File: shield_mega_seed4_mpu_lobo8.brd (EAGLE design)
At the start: 99.4 x 72.4 mm, 32 parts, among them U1 GY-521MPU6050

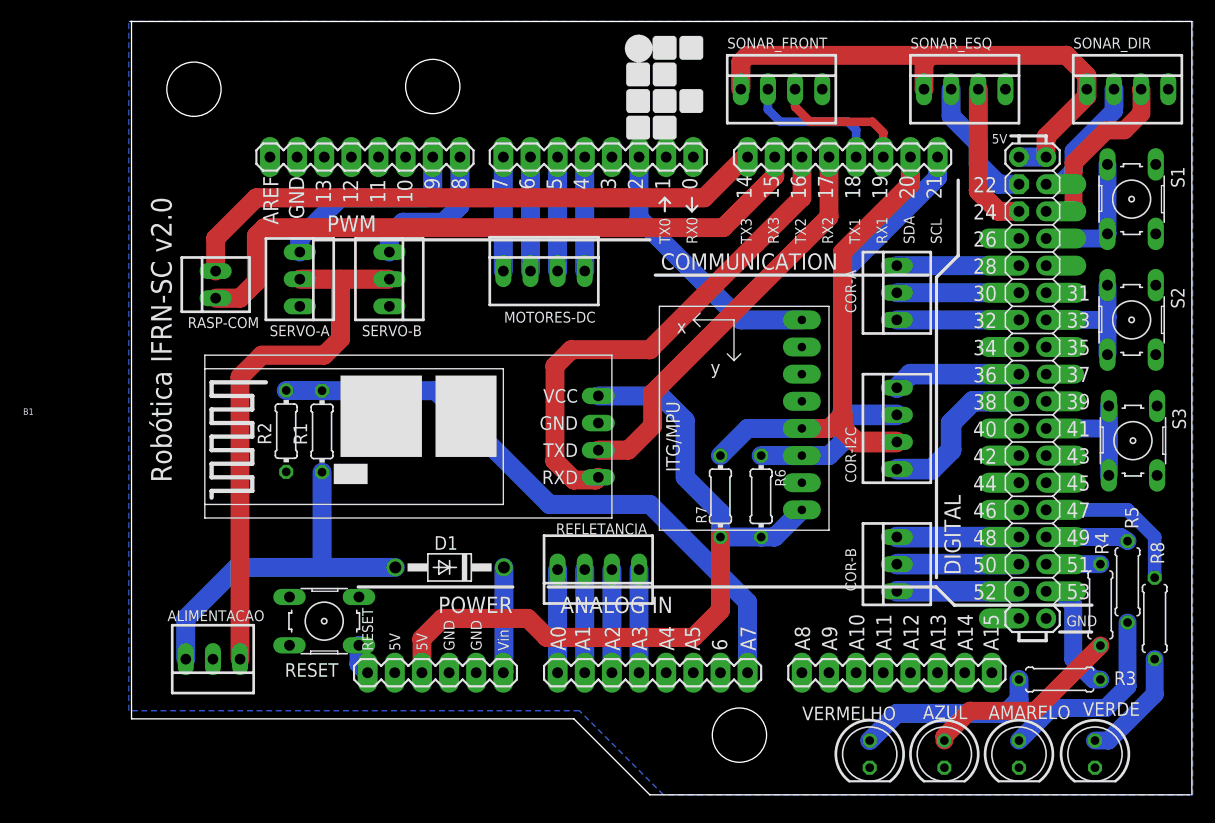
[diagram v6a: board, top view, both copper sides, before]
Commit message: Mudança no tamanho da placa.
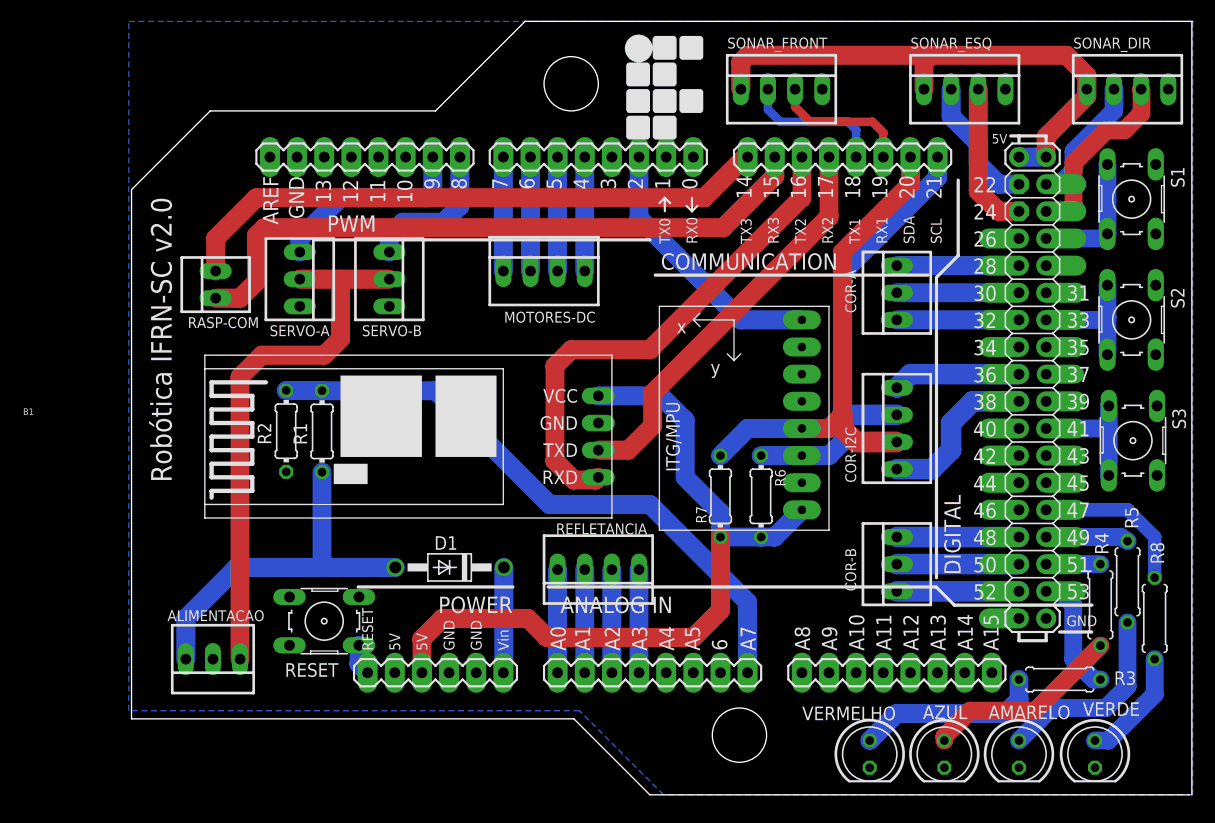
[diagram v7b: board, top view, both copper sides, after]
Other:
- board size 99.4 x 72.4 mm -> 99.3 x 72.4 mm
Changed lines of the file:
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@@
 <layer number="20" name="Dimension" color="15" fill="1" visible="yes" active="yes"/>
 <layer number="21" name="tPlace" color="7" fill="1" visible="yes" active="yes"/>
-<layer number="22" name="bPlace" color="7" fill="1" visible="no" active="yes"/>
+<layer number="22" name="bPlace" color="7" fill="1" visible="yes" active="yes"/>
 <layer number="23" name="tOrigins" color="15" fill="1" visible="yes" active="yes"/>
 <layer number="24" name="bOrigins" color="15" fill="1" visible="yes" active="yes"/>
@@
 <plain>
 <wire x1="98.73" y1="8.89" x2="98.73" y2="81.27" width="0" layer="20"/>
-<wire x1="98.73" y1="81.27" x2="-0.635" y2="81.27" width="0" layer="20"/>
 <rectangle x1="45.9867" y1="70.2183" x2="47.8155" y2="70.2437" layer="21"/>
 <rectangle x1="48.4759" y1="70.2183" x2="50.3047" y2="70.2437" layer="21"/>
@@
 <text x="1.3208" y="64.84111875" size="1.9304" layer="21" font="vector" rot="R270">   Robótica IFRN-SC v2.0</text>
 <hole x="56.388" y="14.478" drill="5.08"/>
-<hole x="27.686" y="75.184" drill="5.08"/>
-<hole x="5.334" y="74.93" drill="5.08"/>
+<hole x="40.64" y="75.438" drill="5.08"/>
 <wire x1="98.552" y1="8.89" x2="48.006" y2="8.89" width="0" layer="20"/>
 <wire x1="48.006" y1="8.89" x2="40.894" y2="16.002" width="0" layer="20"/>
 <wire x1="40.894" y1="16.002" x2="-0.508" y2="16.002" width="0" layer="20"/>
-<wire x1="-0.508" y1="16.002" x2="-0.508" y2="81.28" width="0" layer="20"/>
+<wire x1="-0.508" y1="16.002" x2="-0.508" y2="65.532" width="0" layer="20"/>
+<wire x1="98.806" y1="81.28" x2="36.322" y2="81.28" width="0" layer="20"/>
+<wire x1="6.858" y1="72.898" x2="-0.508" y2="65.532" width="0" layer="20"/>
+<wire x1="27.94" y1="72.898" x2="36.322" y2="81.28" width="0" layer="20"/>
+<wire x1="6.858" y1="72.898" x2="27.94" y2="72.898" width="0" layer="20"/>
 </plain>
 <attributes>

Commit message: Modificação do tamanho mínimo da trilha de terra; Modificação de trilha que estava torta para ficar reta
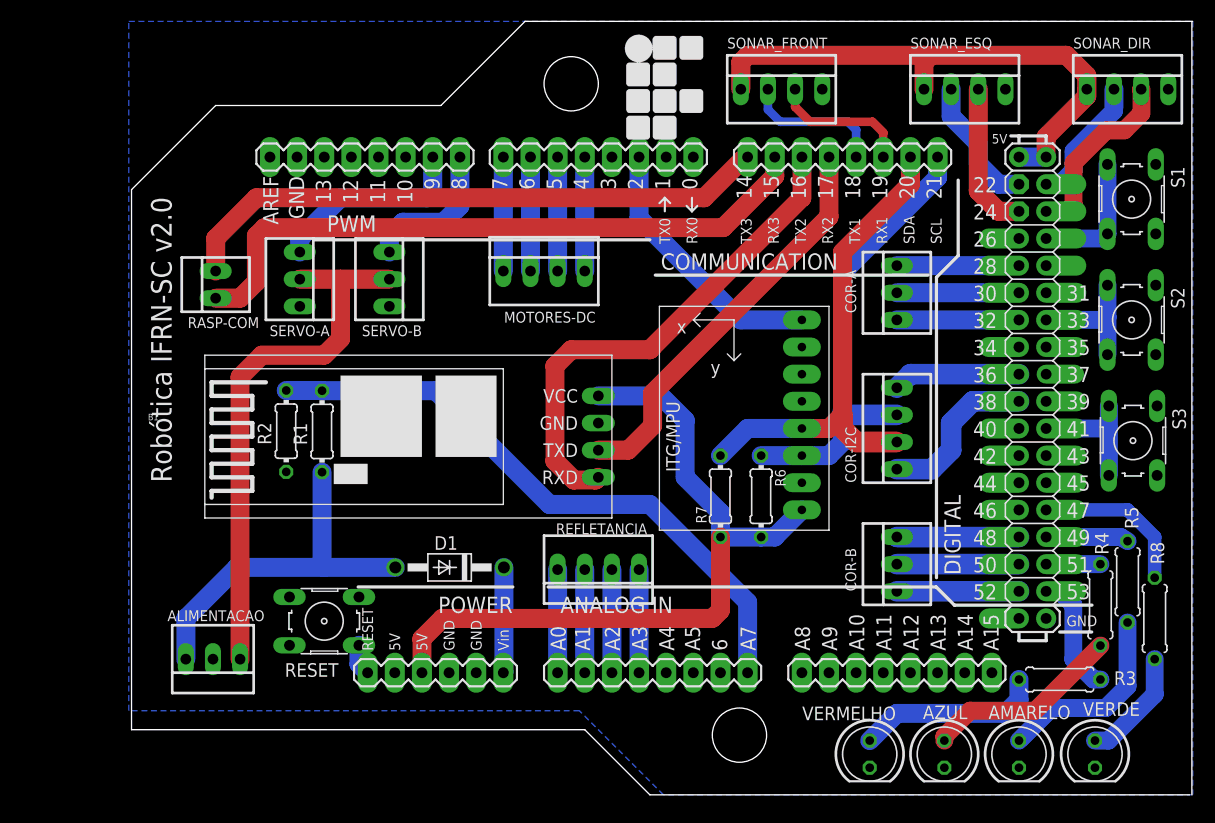
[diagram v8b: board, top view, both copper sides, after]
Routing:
- net +5V/1: track 70.6 -> 69.1 mm
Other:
- outline, holes or cut-outs redrawn
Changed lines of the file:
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@@
 <layer number="20" name="Dimension" color="15" fill="1" visible="yes" active="yes"/>
 <layer number="21" name="tPlace" color="7" fill="1" visible="yes" active="yes"/>
-<layer number="22" name="bPlace" color="7" fill="1" visible="yes" active="yes"/>
+<layer number="22" name="bPlace" color="7" fill="1" visible="no" active="yes"/>
 <layer number="23" name="tOrigins" color="15" fill="1" visible="yes" active="yes"/>
 <layer number="24" name="bOrigins" color="15" fill="1" visible="yes" active="yes"/>
@@
 <hole x="40.64" y="75.438" drill="5.08"/>
 <wire x1="98.552" y1="8.89" x2="48.006" y2="8.89" width="0" layer="20"/>
-<wire x1="48.006" y1="8.89" x2="40.894" y2="16.002" width="0" layer="20"/>
-<wire x1="40.894" y1="16.002" x2="-0.508" y2="16.002" width="0" layer="20"/>
-<wire x1="-0.508" y1="16.002" x2="-0.508" y2="65.532" width="0" layer="20"/>
+<wire x1="48.006" y1="8.89" x2="41.91" y2="14.986" width="0" layer="20"/>
+<wire x1="-0.508" y1="14.986" x2="-0.508" y2="65.532" width="0" layer="20"/>
 <wire x1="98.806" y1="81.28" x2="36.322" y2="81.28" width="0" layer="20"/>
-<wire x1="6.858" y1="72.898" x2="-0.508" y2="65.532" width="0" layer="20"/>
-<wire x1="27.94" y1="72.898" x2="36.322" y2="81.28" width="0" layer="20"/>
-<wire x1="6.858" y1="72.898" x2="27.94" y2="72.898" width="0" layer="20"/>
+<wire x1="7.366" y1="73.406" x2="-0.508" y2="65.532" width="0" layer="20"/>
+<wire x1="28.448" y1="73.406" x2="36.322" y2="81.28" width="0" layer="20"/>
+<wire x1="-0.508" y1="14.986" x2="41.91" y2="14.986" width="0" layer="20"/>
+<wire x1="7.366" y1="73.406" x2="28.448" y2="73.406" width="0" layer="20"/>
 </plain>
 <attributes>
@@
 <elements>
 <element name="B1" library="SparkFun-Boards3" package="ARDUINO_MEGA" value="" x="38.1" y="44.45" locked="yes" smashed="yes">
-<attribute name="NAME" x="-10.16" y="44.45" size="0.6096" layer="25" font="vector" ratio="20" align="bottom-center"/>
+<attribute name="NAME" x="1.524" y="43.942" size="0.6096" layer="25" font="vector" ratio="20" align="bottom-center"/>
 <attribute name="VALUE" x="38.1" y="16.51" size="0.6096" layer="27" font="vector" ratio="20" align="top-center"/>
 </element>
@@
 <contactref element="ALIMENTACAO" pad="2"/>
 <contactref element="B2" pad="3"/>
-<polygon width="0.6096" layer="16">
+<polygon width="0.8128" layer="16">
 <vertex x="-0.762" y="81.28"/>
 <vertex x="98.806" y="81.28"/>
@@
 <wire x1="51.308" y1="43.942" x2="49.022" y2="46.228" width="1.778" layer="16"/>
 <wire x1="49.022" y1="46.228" x2="43.18" y2="46.228" width="1.778" layer="16"/>
-<wire x1="28.575" y1="25.4" x2="36.576" y2="25.4" width="1.778" layer="1"/>
-<wire x1="36.576" y1="25.4" x2="38.354" y2="23.622" width="1.778" layer="1"/>
-<wire x1="38.354" y1="23.622" x2="52.07" y2="23.622" width="1.778" layer="1"/>
-<wire x1="52.07" y1="23.622" x2="54.61" y2="26.162" width="1.778" layer="1"/>
 <wire x1="54.61" y1="26.162" x2="54.61" y2="33.02" width="1.778" layer="1"/>
+<wire x1="28.575" y1="25.4" x2="53.848" y2="25.4" width="1.778" layer="1"/>
+<wire x1="53.848" y1="25.4" x2="54.61" y2="26.162" width="1.778" layer="1"/>
 </signal>
 <signal name="N$14">
